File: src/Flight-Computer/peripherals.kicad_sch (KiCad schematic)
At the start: 30 parts, among them P3 USB, P4 282837-6, Q1 QS5U17TR, Q2 QS5U17TR, U10 RFM95W-868S2, U3 CP2102-GMR(QFN28), U4 SST25VF040B-50-4I-S2AE-T, U5 TS391IYLT, U6 TS391IYLT, U7 TS391IYLT

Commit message: setup layout design rules
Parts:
- Q1, Q2: footprint Package_TO_SOT_THT:TO-92_Inline -> Engine-Controller:QS5U17TR
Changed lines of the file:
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@@
       (effects (font (size 1.27 1.27)) (justify left) hide)
     )
-    (property "Footprint" "Package_TO_SOT_THT:TO-92_Inline" (id 2) (at 199.39 161.29 0)
+    (property "Footprint" "Engine-Controller:QS5U17TR" (id 2) (at 199.39 161.29 0)
       (effects (font (size 1.27 1.27) italic) (justify left) hide)
     )
@@
     (pin "1")
     (pin "2")
+    (pin "3")
+    (pin "4")
     (pin "5")
   )
@@
     (pin "1")
   )
-  (symbol (lib_id "Flight-Computer:QS5U17TR") (at 201.93 102.235 0) (mirror y) (unit 1)
+  (symbol (lib_name "QS5U17TR_1") (lib_id "Flight-Computer:QS5U17TR") (at 201.93 102.235 0) (mirror y) (unit 1)
     (in_bom yes) (on_board yes) (fields_autoplaced)
     (property "Reference" "Q2" (id 0) (at 196.723 102.6688 0)
@@
       (effects (font (size 1.27 1.27)) (justify left) hide)
     )
-    (property "Footprint" "Package_TO_SOT_THT:TO-92_Inline" (id 2) (at 200.025 118.11 0)
+    (property "Footprint" "Engine-Controller:QS5U17TR" (id 2) (at 200.025 118.11 0)
       (effects (font (size 1.27 1.27) italic) (justify left) hide)
     )
@@
     (pin "1")
     (pin "2")
-    (pin "5")
-  )
+    (pin "3")
+    (pin "4")
+    (pin "5")
+  )

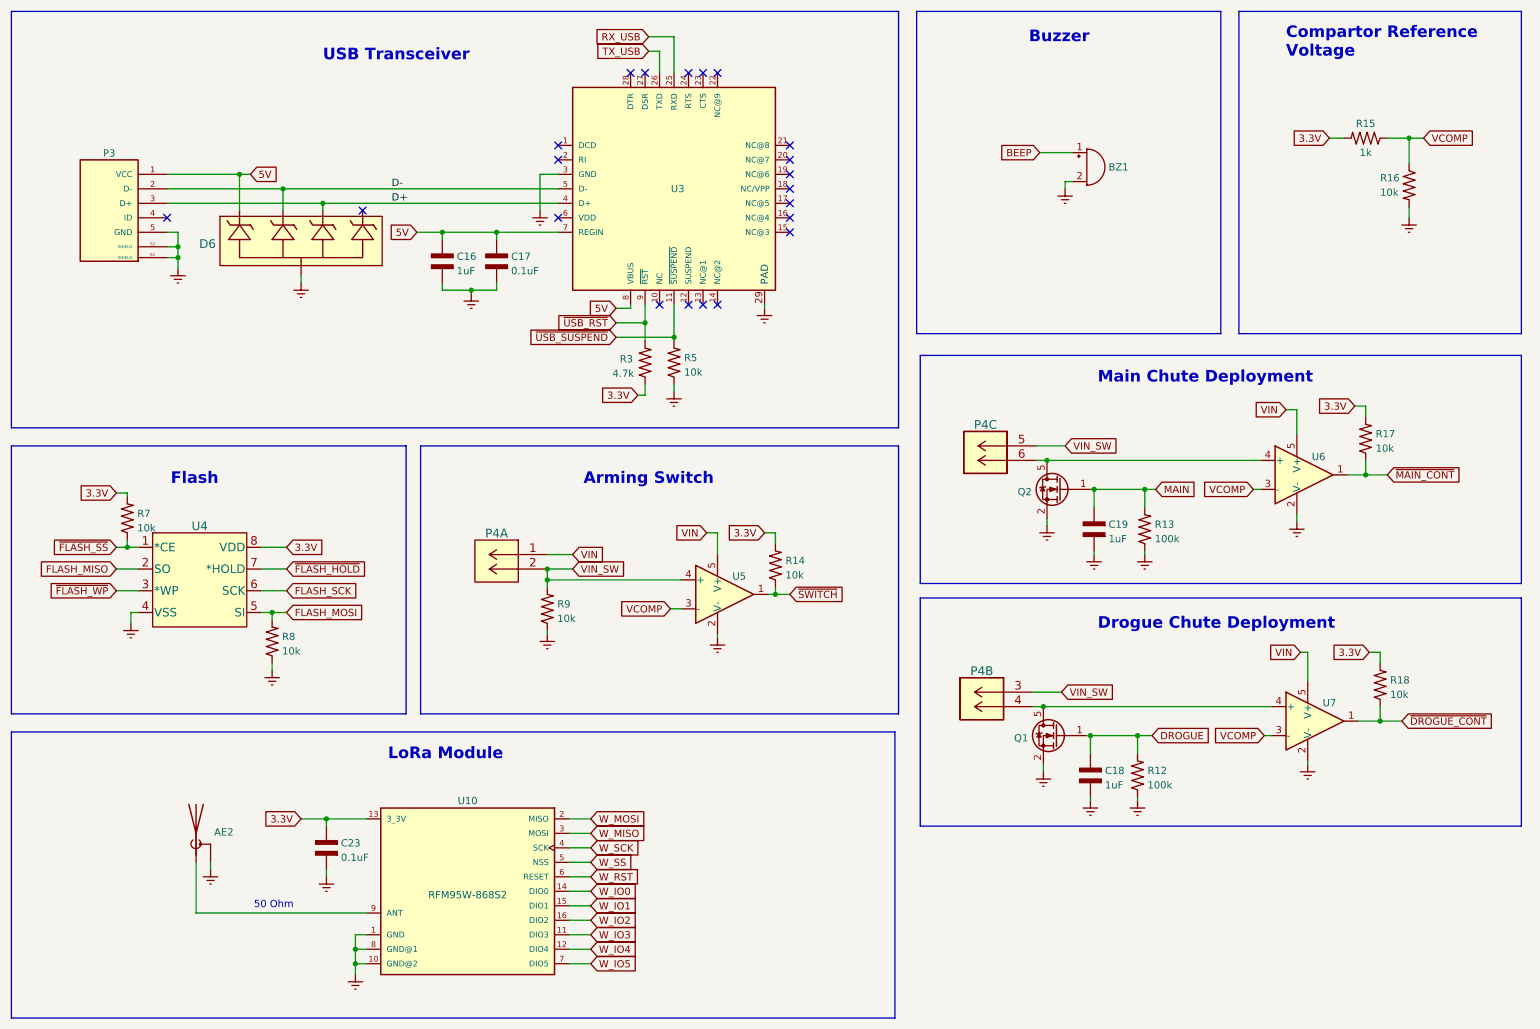
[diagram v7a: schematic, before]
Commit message: placed pcb parts on board and defined form factor
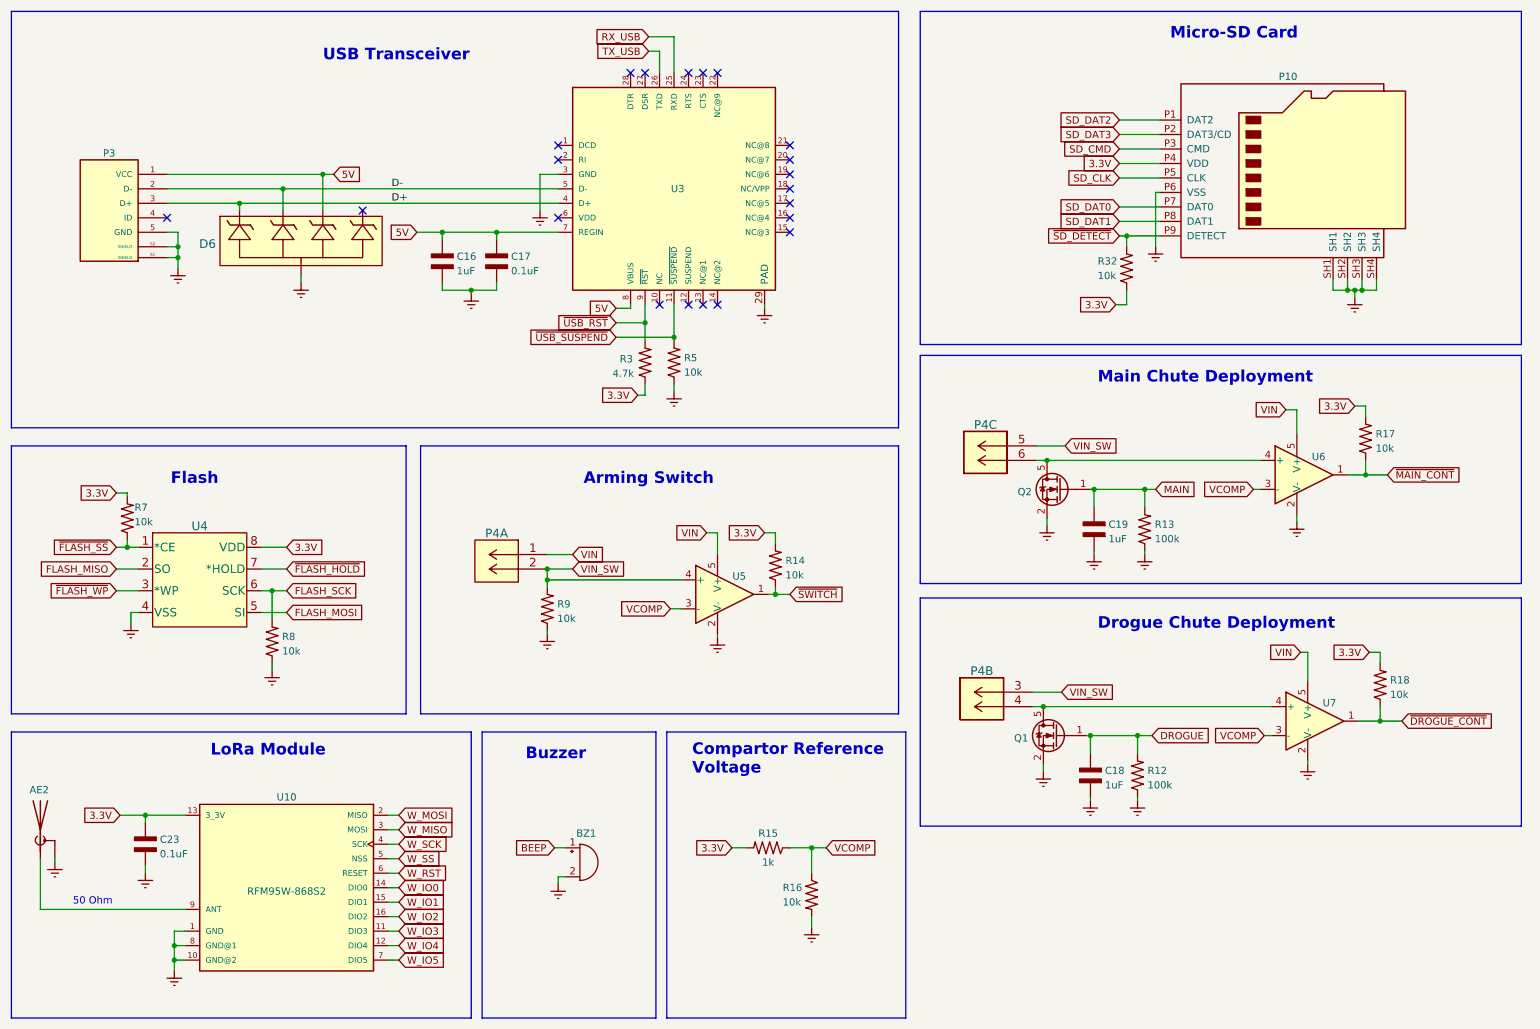
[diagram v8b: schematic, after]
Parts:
- added P10: Micro_SD_Card, Flight-Computer:MEM2075-00-140-01-A, symbol Flight-Computer:Micro_SD_Card
- added R32: 10k, Flight-Computer:RES_0603, symbol Flight-Computer:RES_0603
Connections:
- net 3.3V: now also P10.P4 (VDD), R32.1
- net 5V: now also D6.4; no longer D6.1
- net D+: now also D6.1; no longer D6.4
- net Earth: now also P10.P6 (VSS), P10.SH1, P10.SH2, P10.SH3, P10.SH4
- net FLASH_MOSI: no longer R8.2
- net FLASH_SCK: now also R8.2
- new net SD_CLK: P10.P5 (CLK)
- new net SD_CMD: P10.P3 (CMD)
- new net SD_DAT0: P10.P7 (DAT0)
- new net SD_DAT1: P10.P8 (DAT1)
- new net SD_DAT2: P10.P1 (DAT2)
- new net SD_DAT3: P10.P2 (DAT3/CD)
- new net ~{SD_DETECT}: P10.P9 (DETECT), R32.2
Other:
- note added: "Micro-SD Card"
- moved on the sheet: AE2, BZ1, C23, R15, R16, U10
